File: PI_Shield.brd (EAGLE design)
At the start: 80.1 x 86.7 mm, 68 parts, among them Q1 220mA/50V/3.5Ω, Q3 220mA/50V/3.5Ω, Q4 220mA/50V/3.5Ω, Q5 2.5A/30V/105mΩ, U1 MAX1136EUA-T, U2 AZ1117EH-3.3TRG1, Y1 ECS-80-S-4X

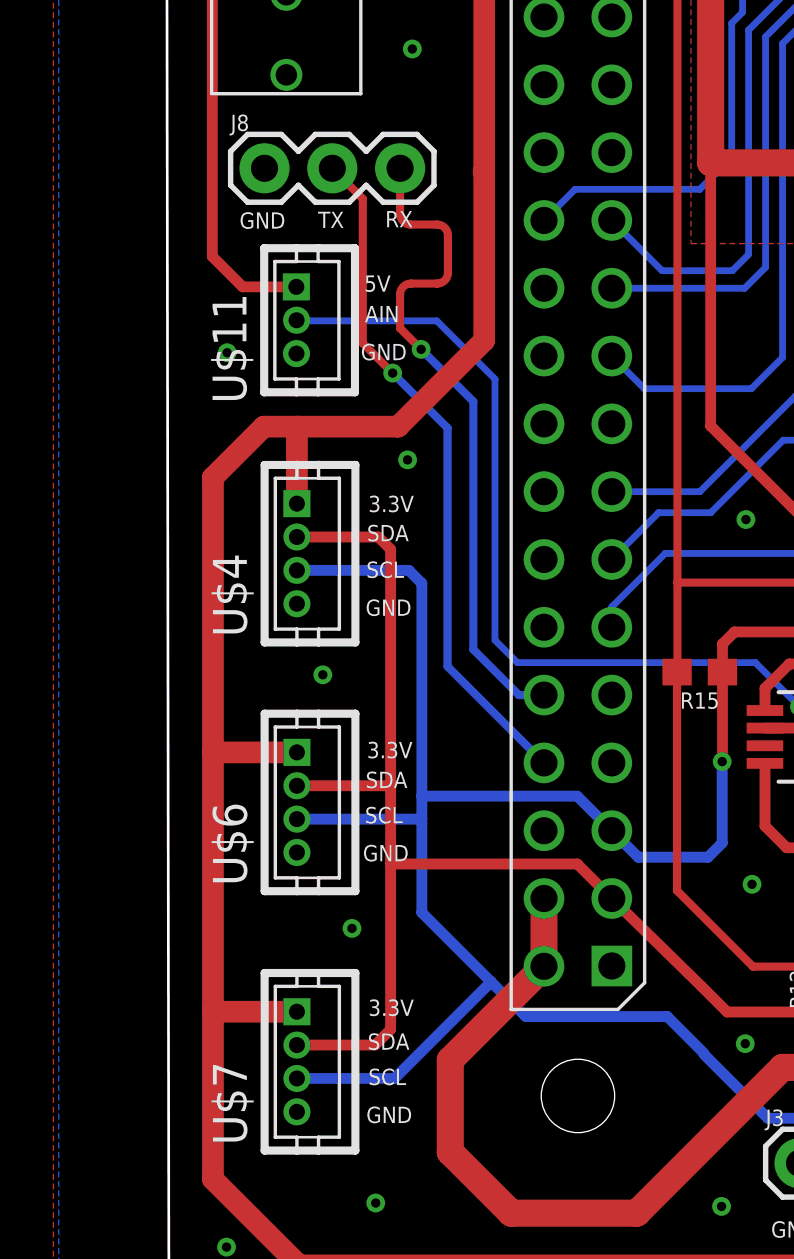
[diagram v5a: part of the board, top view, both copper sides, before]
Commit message: Fixed connector inputs for sensors to match blue robotics website
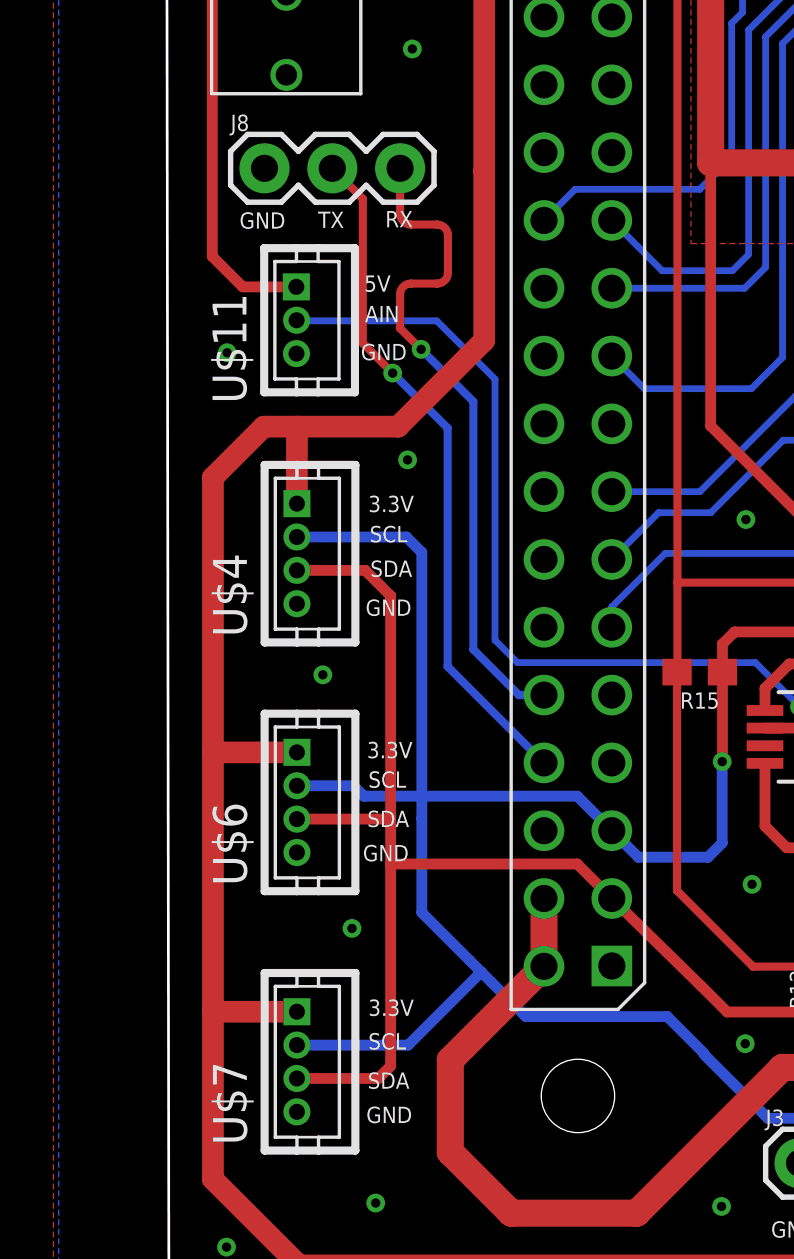
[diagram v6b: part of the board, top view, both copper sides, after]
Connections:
- net SCL: now also U$4.P$2, U$6.P$2, U$7.P$2; no longer U$4.P$3, U$6.P$3, U$7.P$3
- net SDA: now also U$4.P$3, U$6.P$3, U$7.P$3; no longer U$4.P$2, U$6.P$2, U$7.P$2
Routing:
- net SCL: track 133.3 -> 133.9 mm
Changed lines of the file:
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@@
 <?xml version="1.0" encoding="utf-8"?>
 <!DOCTYPE eagle SYSTEM "eagle.dtd">
-<eagle version="9.2.2">
+<eagle version="9.1.3">
 <drawing>
 <settings>
@@
 <layer number="17" name="Pads" color="2" fill="1" visible="yes" active="yes"/>
 <layer number="18" name="Vias" color="2" fill="1" visible="yes" active="yes"/>
-<layer number="19" name="Unrouted" color="6" fill="1" visible="no" active="yes"/>
+<layer number="19" name="Unrouted" color="6" fill="1" visible="yes" active="yes"/>
 <layer number="20" name="Dimension" color="24" fill="1" visible="yes" active="yes"/>
 <layer number="21" name="tPlace" color="7" fill="1" visible="yes" active="yes"/>
@@
 <text x="7.5438" y="18.8214" size="0.6096" layer="21">3.3V</text>
 <text x="7.5946" y="28.0416" size="0.6096" layer="21">3.3V</text>
-<text x="7.5438" y="26.9494" size="0.6096" layer="21">SDA</text>
-<text x="7.493" y="17.7038" size="0.6096" layer="21">SDA</text>
-<text x="7.5692" y="7.8994" size="0.6096" layer="21">SDA</text>
-<text x="7.5946" y="6.5786" size="0.6096" layer="21">SCL</text>
-<text x="7.4676" y="16.383" size="0.6096" layer="21">SCL</text>
-<text x="7.5184" y="25.5778" size="0.6096" layer="21">SCL</text>
+<text x="7.6708" y="25.6159" size="0.6096" layer="21">SDA</text>
+<text x="7.5565" y="16.2433" size="0.6096" layer="21">SDA</text>
+<text x="7.5692" y="6.4389" size="0.6096" layer="21">SDA</text>
+<text x="7.5946" y="7.9121" size="0.6096" layer="21">SCL</text>
+<text x="7.5946" y="17.7165" size="0.6096" layer="21">SCL</text>
+<text x="7.6454" y="26.9113" size="0.6096" layer="21">SCL</text>
 <text x="7.3152" y="33.7312" size="0.6096" layer="21">GND</text>
 <text x="2.7686" y="38.6588" size="0.6096" layer="21">GND</text>
@@
 <contactref element="J6" pad="2"/>
 <contactref element="J7" pad="2"/>
-<wire x1="11.9126" y1="40.7924" x2="11.938" y2="40.8178" width="0.8128" layer="1"/>
 <wire x1="68.6816" y1="13.4112" x2="56.686" y2="13.4112" width="0.8128" layer="16"/>
 <wire x1="56.686" y1="13.4112" x2="56.6606" y2="13.4366" width="0.8128" layer="16"/>
@@
 <contactref element="Q3" pad="2"/>
 <contactref element="R12" pad="1"/>
-<contactref element="U$4" pad="P$2"/>
-<contactref element="U$6" pad="P$2"/>
-<contactref element="U$7" pad="P$2"/>
 <contactref element="R8" pad="2"/>
 <contactref element="J3" pad="3"/>
@@
 <wire x1="30.8229" y1="4.0447" x2="30.4292" y2="3.651" width="0.4064" layer="16" curve="-90"/>
 <wire x1="30.4292" y1="3.651" x2="28.831" y2="3.651" width="0.4064" layer="16"/>
-<wire x1="4.923" y1="27.108" x2="7.9694" y2="27.108" width="0.4064" layer="1"/>
-<wire x1="7.9694" y1="27.108" x2="8.4328" y2="26.6446" width="0.4064" layer="1"/>
-<wire x1="8.4328" y1="8.6614" x2="7.8486" y2="8.0772" width="0.4064" layer="1"/>
-<wire x1="7.8486" y1="8.0772" x2="4.9252" y2="8.0772" width="0.4064" layer="1"/>
-<wire x1="4.9252" y1="8.0772" x2="4.923" y2="8.075" width="0.4064" layer="1"/>
-<wire x1="8.4328" y1="26.6446" x2="8.4328" y2="17.78" width="0.4064" layer="1"/>
-<wire x1="8.4328" y1="17.78" x2="8.4328" y2="14.8336" width="0.4064" layer="1"/>
-<wire x1="8.4328" y1="14.8336" x2="8.4328" y2="8.6614" width="0.4064" layer="1"/>
-<wire x1="4.923" y1="17.79" x2="8.4228" y2="17.79" width="0.4064" layer="1"/>
-<wire x1="8.4228" y1="17.79" x2="8.4328" y2="17.78" width="0.4064" layer="1"/>
+<wire x1="8.4328" y1="17.78" x2="8.4328" y2="16.51" width="0.4064" layer="1"/>
+<wire x1="8.4328" y1="16.51" x2="8.4328" y2="14.8336" width="0.4064" layer="1"/>
 <wire x1="15.4258" y1="14.859" x2="8.4582" y2="14.859" width="0.4064" layer="1"/>
 <wire x1="8.4582" y1="14.859" x2="8.4328" y2="14.8336" width="0.4064" layer="1"/>
+<contactref element="U$4" pad="P$3"/>
+<contactref element="U$6" pad="P$3"/>
+<contactref element="U$7" pad="P$3"/>
+<wire x1="4.923" y1="16.54" x2="8.4028" y2="16.54" width="0.4064" layer="1"/>
+<wire x1="8.4028" y1="16.54" x2="8.4328" y2="16.51" width="0.4064" layer="1"/>
+<wire x1="4.923" y1="25.858" x2="7.4795" y2="25.858" width="0.4064" layer="1"/>
+<wire x1="8.4328" y1="24.9047" x2="8.4328" y2="17.78" width="0.4064" layer="1"/>
+<wire x1="7.4795" y1="25.858" x2="8.4328" y2="24.9047" width="0.4064" layer="1"/>
+<wire x1="4.923" y1="6.825" x2="7.968" y2="6.825" width="0.4064" layer="1"/>
+<wire x1="7.968" y1="6.825" x2="8.4328" y2="7.2898" width="0.4064" layer="1"/>
+<wire x1="8.4328" y1="7.2898" x2="8.4328" y2="14.8336" width="0.4064" layer="1"/>
 </signal>
 <signal name="SCL">
@@
 <contactref element="Q1" pad="2"/>
 <contactref element="R15" pad="1"/>
-<contactref element="U$4" pad="P$3"/>
-<contactref element="U$6" pad="P$3"/>
-<contactref element="U$7" pad="P$3"/>
 <contactref element="R9" pad="2"/>
 <contactref element="J3" pad="2"/>
@@
 <wire x1="16.7182" y1="16.1066" x2="15.4258" y2="17.399" width="0.4064" layer="16"/>
 <wire x1="12.19621875" y1="10.44361875" x2="13.4958375" y2="9.144" width="0.4064" layer="16"/>
-<wire x1="4.923" y1="6.825" x2="8.5776" y2="6.825" width="0.4064" layer="16"/>
 <via x="50.038" y="3.937" extent="1-16" drill="0.35"/>
 <wire x1="50.038" y1="4.572" x2="50.038" y2="3.937" width="0.4064" layer="1"/>
@@
 <wire x1="20.8534" y1="15.6464" x2="20.32" y2="15.113" width="0.4064" layer="16"/>
 <wire x1="54.389" y1="11.557" x2="71.9074" y2="11.557" width="0.4064" layer="1"/>
-<wire x1="8.5776" y1="6.825" x2="12.19621875" y2="10.44361875" width="0.4064" layer="16"/>
 <wire x1="20.8632" y1="23.0984" x2="20.8632" y2="22.0482" width="0.4064" layer="1"/>
 <wire x1="20.8632" y1="22.0482" x2="20.8632" y2="18.7042" width="0.4064" layer="1"/>
@@
 <via x="20.8534" y="18.6944" extent="1-16" drill="0.35"/>
 <wire x1="20.8534" y1="18.6944" x2="20.8534" y2="15.6464" width="0.4064" layer="16"/>
-<wire x1="4.923" y1="25.858" x2="9.1178" y2="25.858" width="0.4064" layer="16"/>
-<wire x1="9.1178" y1="25.858" x2="9.6012" y2="25.3746" width="0.4064" layer="16"/>
-<wire x1="9.6012" y1="25.3746" x2="9.6012" y2="17.399" width="0.4064" layer="16"/>
 <wire x1="9.6012" y1="17.399" x2="9.6012" y2="16.5608" width="0.4064" layer="16"/>
 <wire x1="9.6012" y1="16.5608" x2="9.6012" y2="13.0386375" width="0.4064" layer="16"/>
-<wire x1="9.6012" y1="13.0386375" x2="12.19621875" y2="10.44361875" width="0.4064" layer="16"/>
-<wire x1="4.923" y1="16.54" x2="9.5804" y2="16.54" width="0.4064" layer="16"/>
-<wire x1="9.5804" y1="16.54" x2="9.6012" y2="16.5608" width="0.4064" layer="16"/>
+<wire x1="9.6012" y1="13.0386375" x2="11.41516875" y2="11.22466875" width="0.4064" layer="16"/>
+<wire x1="11.82791875" y1="10.81191875" x2="12.19621875" y2="10.44361875" width="0.4064" layer="16"/>
 <wire x1="15.4258" y1="17.399" x2="9.6012" y2="17.399" width="0.4064" layer="16"/>
+<contactref element="U$4" pad="P$2"/>
+<contactref element="U$6" pad="P$2"/>
+<contactref element="U$7" pad="P$2"/>
+<wire x1="9.0235" y1="27.108" x2="4.923" y2="27.108" width="0.4064" layer="16"/>
+<wire x1="9.6012" y1="17.399" x2="9.6012" y2="26.5303" width="0.4064" layer="16"/>
+<wire x1="9.6012" y1="26.5303" x2="9.0235" y2="27.108" width="0.4064" layer="16"/>
+<wire x1="4.923" y1="8.075" x2="9.091" y2="8.075" width="0.4064" layer="16"/>
+<wire x1="9.091" y1="8.075" x2="11.82791875" y2="10.81191875" width="0.4064" layer="16"/>
+<wire x1="4.923" y1="17.79" x2="7.0385" y2="17.79" width="0.4064" layer="16"/>
+<wire x1="7.4295" y1="17.399" x2="9.6012" y2="17.399" width="0.4064" layer="16"/>
+<wire x1="7.0385" y1="17.79" x2="7.4295" y2="17.399" width="0.4064" layer="16"/>
+<wire x1="11.41516875" y1="11.22466875" x2="11.82791875" y2="10.81191875" width="0.4064" layer="16"/>
 </signal>
 <signal name="IMU_RESET">

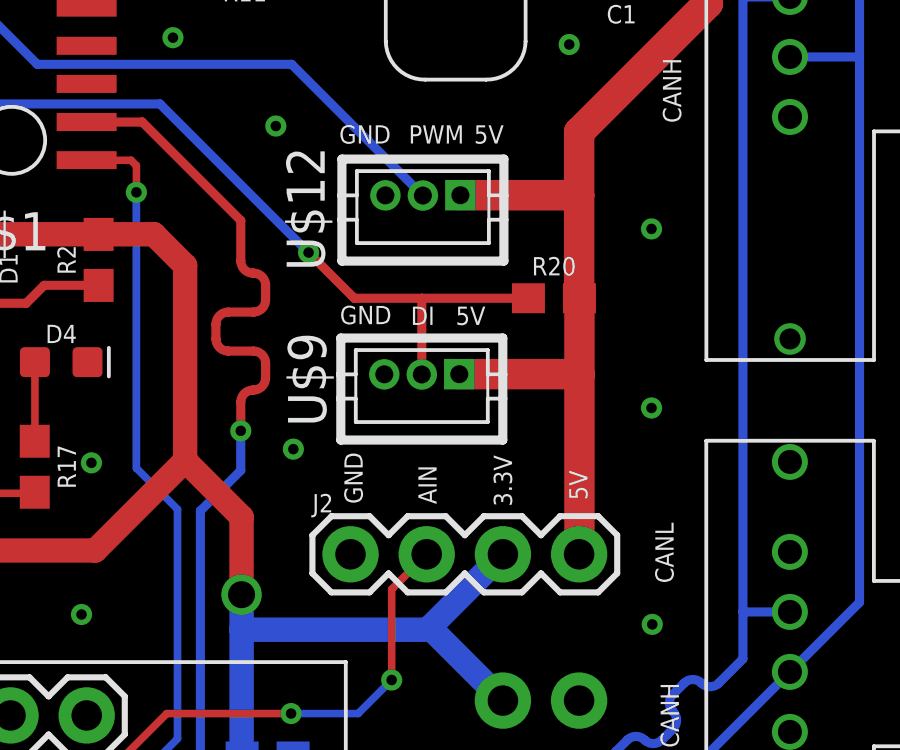
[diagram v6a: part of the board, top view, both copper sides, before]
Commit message: switched power from 5v to 3.3v on dallas temperature sensor
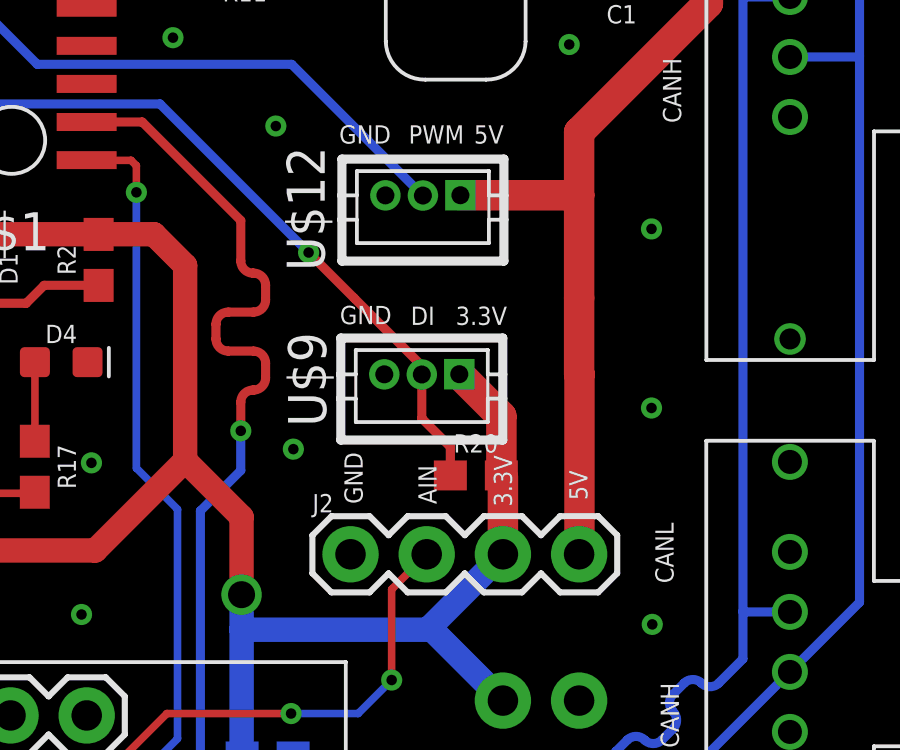
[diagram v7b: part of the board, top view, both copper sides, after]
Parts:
- moved R20 6.45 mm to (64.5, 34.4)
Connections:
- net 3V3: now also R20.2, U$9.P$1
- net 5V: no longer R20.2, U$9.P$1
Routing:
- net 3V3: track 391.3 -> 397.9 mm
- net 5V: track 292.6 -> 288.6 mm
- net DI: track 57.2 -> 56.1 mm
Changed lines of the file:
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@@
 <text x="59.9186" y="39.4716" size="0.6096" layer="21">GND</text>
 <text x="62.2808" y="39.4462" size="0.6096" layer="21">DI</text>
-<text x="63.7794" y="39.4462" size="0.6096" layer="21">5V</text>
+<text x="63.7794" y="39.4462" size="0.6096" layer="21">3.3V</text>
 <text x="72.2376" y="61.595" size="0.6096" layer="21" rot="R90">CANH</text>
 <text x="71.2978" y="46.1772" size="0.6096" layer="21" rot="R90">CANH</text>
@@
 <attribute name="VALUE" x="56.746" y="55.488" size="0.6096" layer="27" font="vector" ratio="20" rot="R180" align="top-center"/>
 </element>
-<element name="R20" library="SparkFun-Resistors" library_urn="urn:adsk.eagle:library:532" package="0603" package3d_urn="urn:adsk.eagle:package:39650/1" value="4.7k" x="67.056" y="40.3352" smashed="yes">
-<attribute name="NAME" x="67.056" y="41.0972" size="0.6096" layer="25" font="vector" ratio="20" align="bottom-center"/>
-<attribute name="PROD_ID" value=" " x="67.31" y="40.3352" size="1.778" layer="27" display="off"/>
-<attribute name="VALUE" x="67.056" y="39.5732" size="0.6096" layer="27" font="vector" ratio="20" align="top-center"/>
+<element name="R20" library="SparkFun-Resistors" library_urn="urn:adsk.eagle:library:532" package="0603" package3d_urn="urn:adsk.eagle:package:39650/1" value="4.7k" x="64.4525" y="34.4297" smashed="yes">
+<attribute name="NAME" x="64.4525" y="35.1917" size="0.6096" layer="25" font="vector" ratio="20" align="bottom-center"/>
+<attribute name="PROD_ID" value=" " x="64.7065" y="34.4297" size="1.778" layer="27" display="off"/>
+<attribute name="VALUE" x="64.4525" y="33.6677" size="0.6096" layer="27" font="vector" ratio="20" align="top-center"/>
 </element>
 <element name="U$12" library="con-hirose-df13" package="DF13-3P-1.25DSA" value="DF13-3P-1.25DSA" x="62.6872" y="43.7642" smashed="yes">
@@
 <wire x1="55.5822" y1="2.928" x2="56.642" y2="3.9878" width="0.8128" layer="1"/>
 <wire x1="56.642" y1="3.9878" x2="56.642" y2="8.2804" width="0.8128" layer="1"/>
+<contactref element="U$9" pad="P$1"/>
+<contactref element="R20" pad="2"/>
+<wire x1="65.3542" y1="31.8008" x2="65.3542" y2="34.378" width="1.016" layer="1"/>
+<wire x1="65.3542" y1="34.378" x2="65.3025" y2="34.4297" width="1.016" layer="1"/>
+<wire x1="65.3025" y1="34.4297" x2="65.3025" y2="36.4017" width="1.016" layer="1"/>
+<wire x1="65.3025" y1="36.4017" x2="63.9002" y2="37.804" width="1.016" layer="1"/>
 </signal>
 <signal name="N$4">
@@
 <contactref element="U2" pad="3"/>
 <contactref element="C11" pad="1"/>
-<contactref element="U$9" pad="P$1"/>
 <wire x1="59.69" y1="60.198" x2="68.6816" y2="60.198" width="1.016" layer="1"/>
 <wire x1="68.6816" y1="60.198" x2="75.196" y2="66.7124" width="1.016" layer="1"/>
@@
 </polygon>
 <wire x1="24.511" y1="35.56399375" x2="24.50200625" y2="35.555" width="1.016" layer="1"/>
-<contactref element="R20" pad="2"/>
 <polygon width="0.3048" layer="1">
 <vertex x="8.763" y="63.5254"/>
@@
 <wire x1="63.9372" y1="43.7692" x2="67.8942" y2="43.7692" width="1.016" layer="1"/>
 <wire x1="5.0372" y1="68.9738" x2="5.0372" y2="66.9738" width="1.016" layer="1"/>
-<wire x1="67.8942" y1="43.7692" x2="67.8942" y2="40.347" width="1.016" layer="1"/>
-<wire x1="67.8942" y1="40.347" x2="67.906" y2="40.3352" width="1.016" layer="1"/>
+<wire x1="67.8942" y1="40.347" x2="67.8942" y2="43.7692" width="1.016" layer="1"/>
 <wire x1="67.906" y1="31.8126" x2="67.8942" y2="31.8008" width="1.016" layer="1"/>
-<wire x1="67.906" y1="40.3352" x2="67.906" y2="37.7952" width="1.016" layer="1"/>
 <wire x1="67.906" y1="37.7952" x2="67.906" y2="31.8126" width="1.016" layer="1"/>
-<wire x1="63.9002" y1="37.804" x2="67.8972" y2="37.804" width="1.016" layer="1"/>
-<wire x1="67.8972" y1="37.804" x2="67.906" y2="37.7952" width="1.016" layer="1"/>
+<wire x1="67.906" y1="37.7952" x2="67.8972" y2="37.804" width="1.016" layer="1"/>
 <wire x1="26.8254" y1="20.6096" x2="30.6936" y2="20.6096" width="0.4064" layer="1"/>
 <wire x1="30.6936" y1="20.6096" x2="30.878" y2="20.794" width="0.4064" layer="1"/>
@@
 <wire x1="2.892" y1="36.478" x2="4.901" y2="36.478" width="0.4064" layer="1"/>
 <wire x1="1.7526" y1="37.6174" x2="2.892" y2="36.478" width="0.4064" layer="1"/>
+<wire x1="67.8972" y1="37.804" x2="67.8942" y2="37.807" width="0.762" layer="1"/>
+<wire x1="67.8942" y1="37.807" x2="67.8942" y2="40.347" width="1.016" layer="1"/>
 </signal>
 <signal name="AIN">
@@
 <wire x1="53.9242" y1="46.8122" x2="58.8772" y2="41.8592" width="0.3048" layer="16"/>
 <via x="58.8772" y="41.8592" extent="1-16" drill="0.35"/>
-<wire x1="60.4012" y1="40.3352" x2="58.8772" y2="41.8592" width="0.3048" layer="1"/>
+<wire x1="58.8772" y1="41.8592" x2="60.4012" y2="40.3352" width="0.3048" layer="1"/>
 <wire x1="34.925" y1="46.8122" x2="33.147" y2="48.5902" width="0.3048" layer="16"/>
 <wire x1="34.925" y1="46.8122" x2="53.9242" y2="46.8122" width="0.3048" layer="16"/>
-<wire x1="66.206" y1="40.3352" x2="62.6618" y2="40.3352" width="0.3048" layer="1"/>
-<wire x1="62.6618" y1="40.3352" x2="60.4012" y2="40.3352" width="0.3048" layer="1"/>
-<wire x1="62.6502" y1="37.794" x2="62.6502" y2="40.3236" width="0.3048" layer="1"/>
-<wire x1="62.6502" y1="40.3236" x2="62.6618" y2="40.3352" width="0.3048" layer="1"/>
+<wire x1="63.6025" y1="35.3812" x2="63.6025" y2="34.4297" width="0.3048" layer="1"/>
 <wire x1="33.147" y1="48.5902" x2="27.6352" y2="48.5902" width="0.3048" layer="16"/>
 <via x="27.6352" y="48.5902" extent="1-16" drill="0.35"/>
@@
 <wire x1="24.7396" y1="50.9778" x2="18.5694" y2="50.9778" width="0.3048" layer="16"/>
 <wire x1="18.5694" y1="50.9778" x2="16.7182" y2="49.1266" width="0.3048" layer="16"/>
+<wire x1="62.6502" y1="37.794" x2="62.65" y2="37.7938" width="0.3048" layer="1"/>
+<wire x1="60.4012" y1="40.3352" x2="62.65" y2="38.0864" width="0.3048" layer="1"/>
+<wire x1="62.65" y1="38.0864" x2="62.65" y2="37.7938" width="0.254" layer="1"/>
+<wire x1="62.6502" y1="36.3335" x2="63.6025" y2="35.3812" width="0.3048" layer="1"/>
+<wire x1="62.6502" y1="37.794" x2="62.6502" y2="36.3335" width="0.3048" layer="1"/>
 </signal>
 <signal name="OSC2_XTAL">
